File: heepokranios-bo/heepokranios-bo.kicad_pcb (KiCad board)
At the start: 4 copper layers, 150.1 x 168.4 mm, 242 parts, among them IC1 ADA4945-1ACPZ-R7, IC2 ADA4945-1ACPZ-R7, IC3 ADA4945-1ACPZ-R7, IC4 ADA4945-1ACPZ-R7, IC5 ADA4945-1ACPZ-R7, J1 Conn_02x02_Odd_Even, J11 PGA_13x13, J14 Conn_02x03_Odd_Even, J15 Conn_02x08_Odd_Even, J16 Conn_02x03_Odd_Even, J17 Conn_02x03_Odd_Even, J18 Conn_01x03, J19 Conn_01x03, J2 Conn_02x02_Odd_Even, J20 Conn_01x03, J21 Conn_01x02, J22 Conn_01x03, J23 Conn_02x02_Odd_Even, J24 Conn_02x02_Odd_Even, J25 Conn_02x02_Odd_Even, J26 Conn_01x02, J27 Conn_01x02, J28 Conn_02x02_Odd_Even, J29 Conn_01x02, J3 Conn_02x03_Odd_Even, J30 Conn_01x02, J31 Conn_01x02, J32 Conn_01x02, J33 Conn_01x02, J34 Conn_01x02, J35 Conn_01x02, J36 Conn_01x02, J37 Conn_01x02, J38 Conn_01x02, J39 Conn_01x02, J4 Conn_02x03_Odd_Even, J40 Conn_01x02, J41 Conn_01x02, J42 Conn_01x02, J43 Conn_01x02, J44 Conn_02x02_Odd_Even, J45 Conn_01x03, J48 Conn_01x02, J49 Conn_01x02, J5 Conn_02x03_Odd_Even, J6 Conn_02x04_Odd_Even, J8 Conn_02x03_Odd_Even, J9 Conn_02x02_Odd_Even, SW1 SW_Push, U1 BIWIN_DTS04GE_SMD

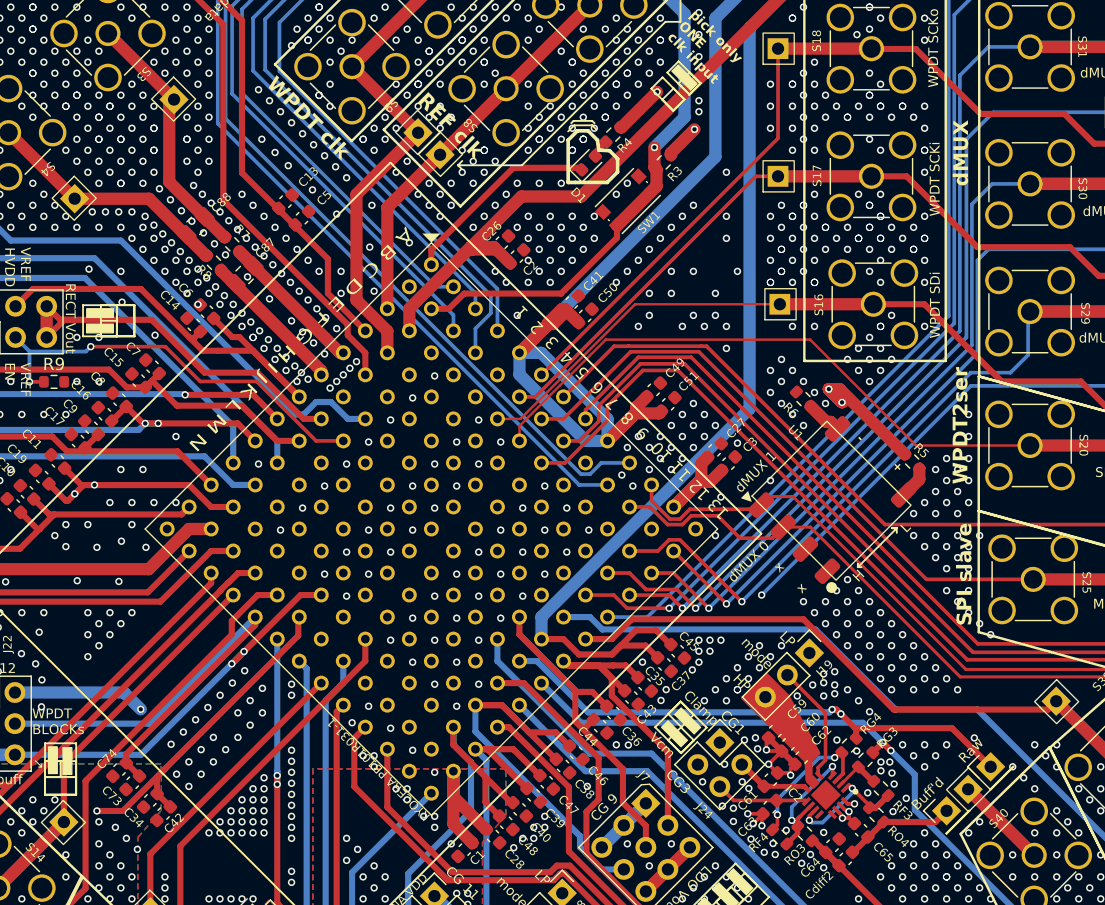
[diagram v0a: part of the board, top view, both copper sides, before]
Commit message: Re-routed dMUX 0-7 pins from chip as they were inverted
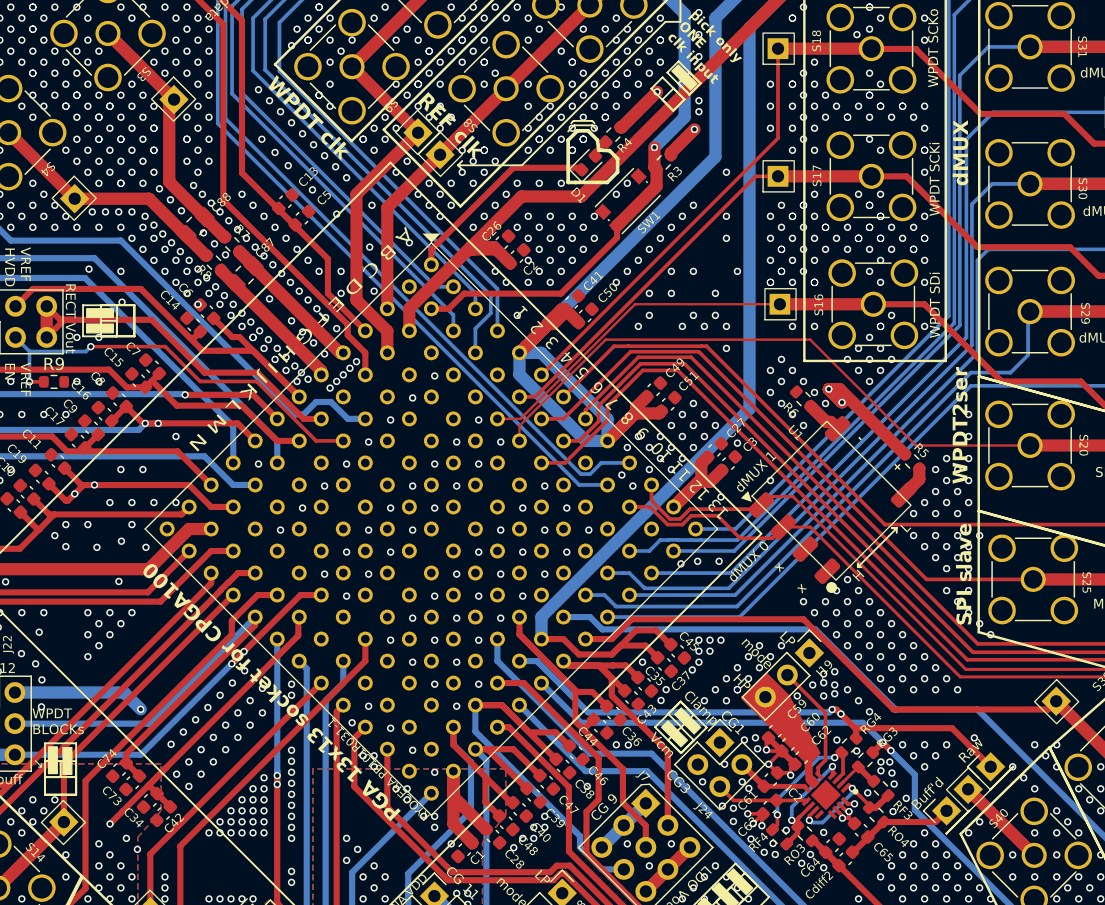
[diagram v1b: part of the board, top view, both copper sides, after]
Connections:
- J11 pad A13: /DMUX_0 -> /DMUX_7
- J11 pad B13: /DMUX_2 -> /DMUX_5
- J11 pad C12: /DMUX_1 -> /DMUX_6
- J11 pad C13: /DMUX_3 -> /DMUX_4
- J11 pad D12: /DMUX_4 -> /DMUX_3
- J11 pad D13: /DMUX_5 -> /DMUX_2
- J11 pad E12: /DMUX_6 -> /DMUX_1
- J11 pad E13: /DMUX_7 -> /DMUX_0
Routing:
- net /DMUX_0: track 62.6 -> 75.9 mm, vias 1 -> 0
- net /DMUX_7: track 119.5 -> 109.3 mm
- net /DMUX_5: track 103.6 -> 97.4 mm, vias 1 -> 0
- net /DMUX_4: track 97.7 -> 91.8 mm, vias 1 -> 0
- net /DMUX_6: track 113.9 -> 108.0 mm, vias 1 -> 0
- net /DMUX_3: track 87.2 -> 89.4 mm, vias 1 -> 0
- net /DMUX_1: track 79.1 -> 80.8 mm, vias 1 -> 0
- net /DMUX_2: track 80.1 -> 81.6 mm, vias 1 -> 0
- net /LNA_VCM_VIN: track 39.9 -> 41.3 mm
- net GND: vias 3428 -> 3425
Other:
- board text added: "PGA 13x13 socket for CPGA100"
